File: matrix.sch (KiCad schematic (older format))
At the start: 126 parts

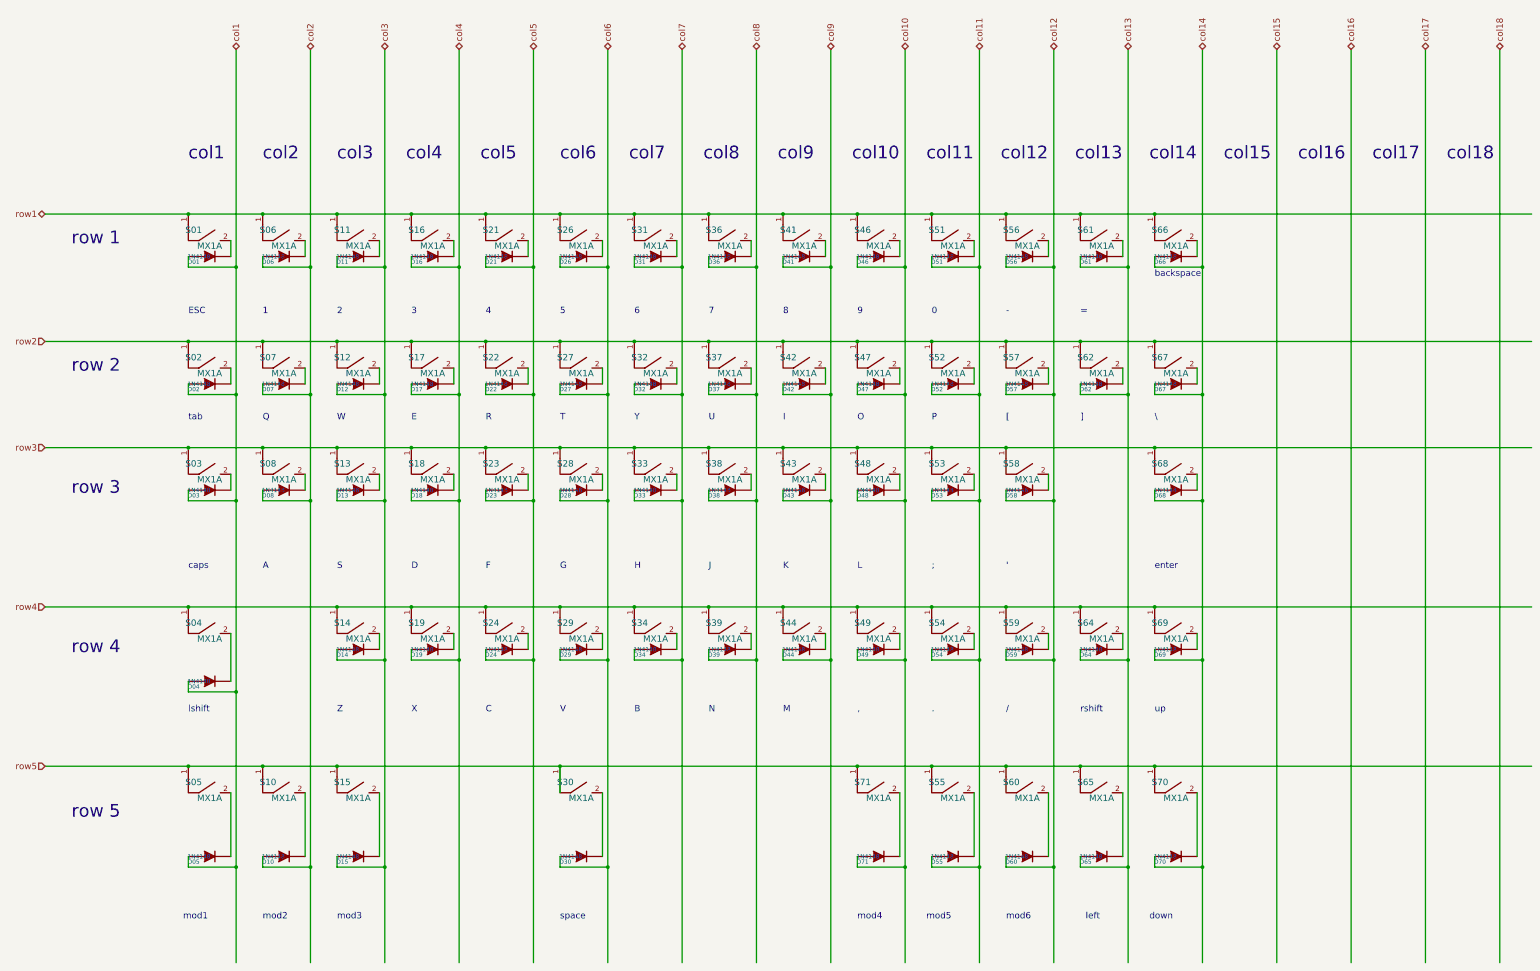
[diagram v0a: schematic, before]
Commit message: Optimise matrix to save an additional pin on the MCU
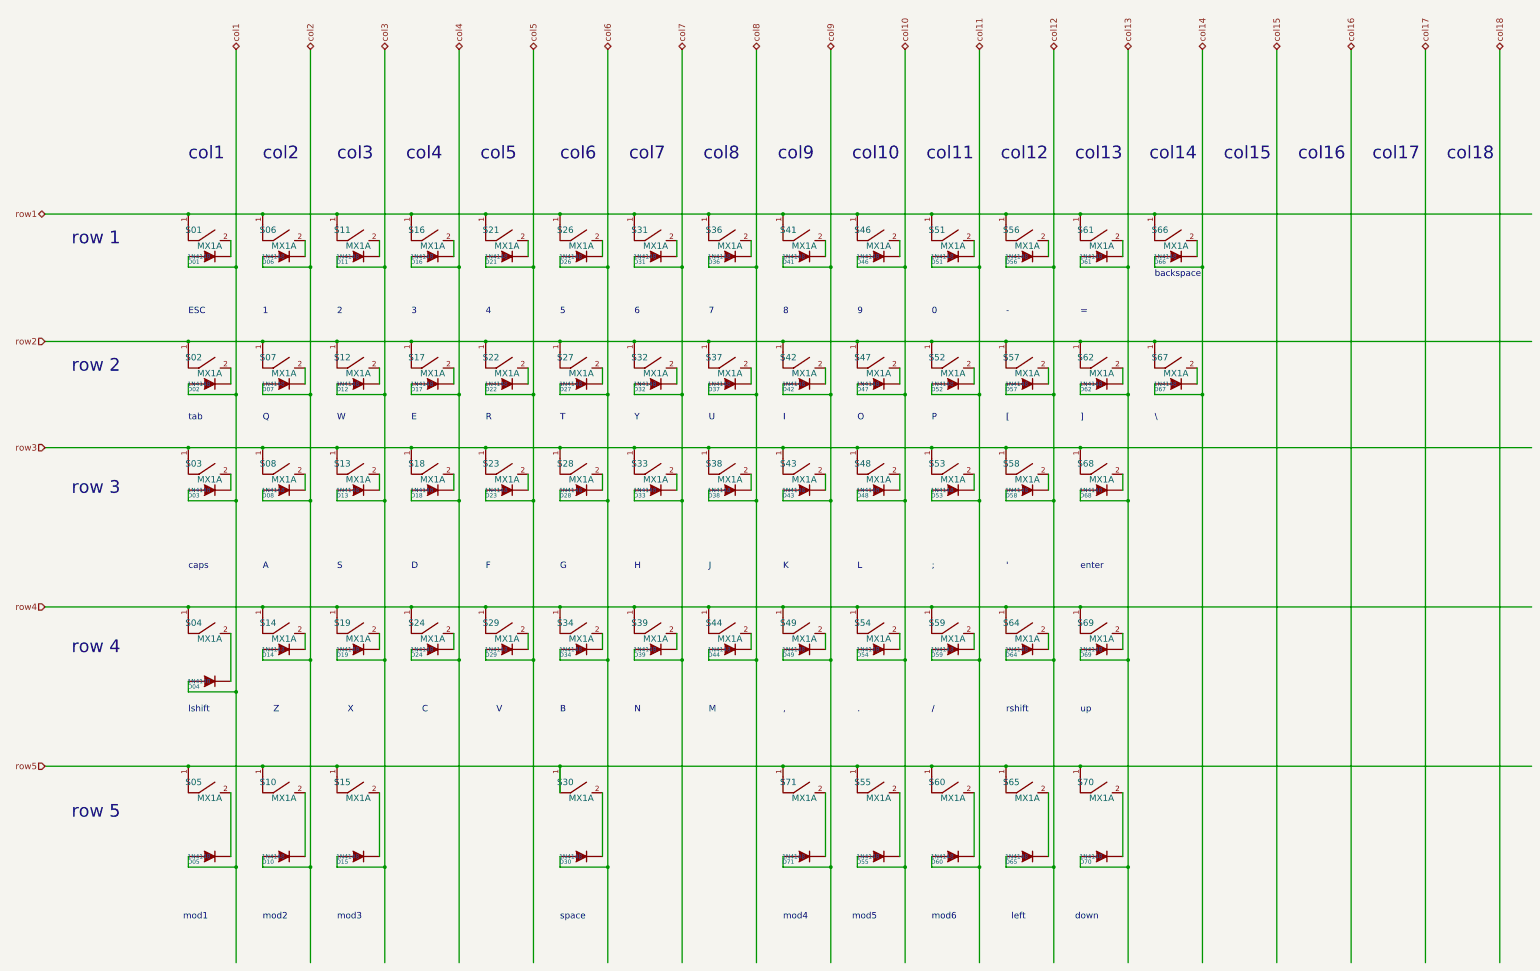
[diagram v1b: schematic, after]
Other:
- moved on the sheet: D14, D19, D24, D29, D34, D39, D44, D49, D54, D55, D59, D60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

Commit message: PCB with 3 pins ready for backlight
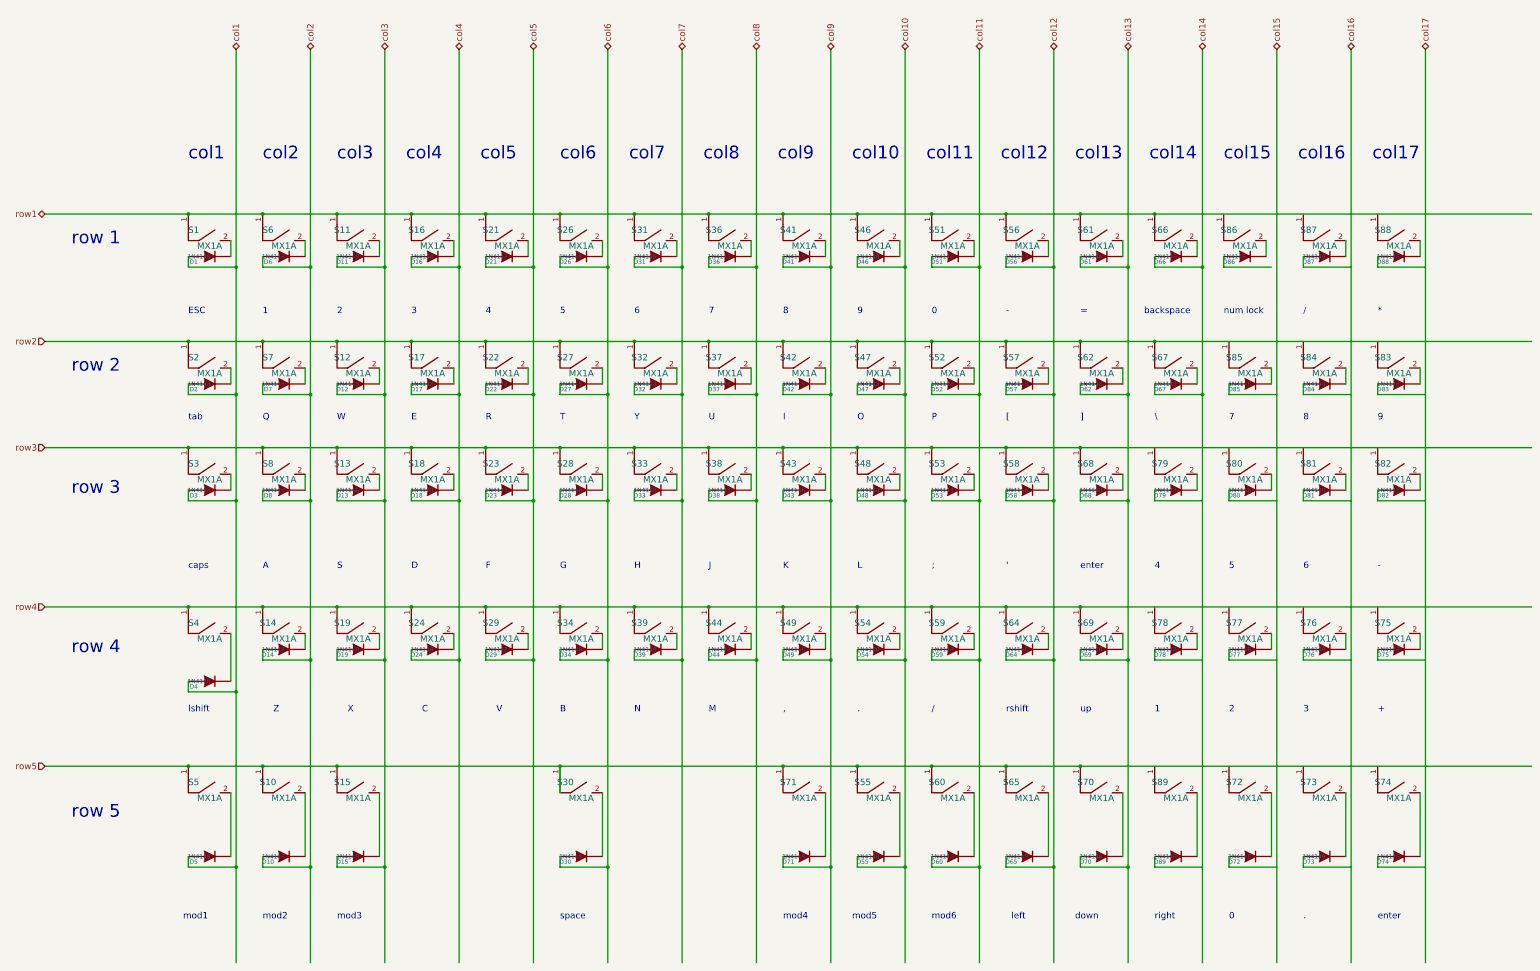
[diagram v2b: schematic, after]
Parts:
- added D72, D73, D74, D75, D76, D77, D78, D79, D80, D81, D82, D83, D84, D85, D86, D87, D88, D89: 1N4148, 0805:0805D, symbol device:DIODE
- added S72, S73, S74, S75, S76, S77, S78, S79, S80, S81, S82, S83, S84, S85, S86, S87, S88, S89: MX1A, mx1a:MX1A, symbol mx1a-simple:MX1A
- renumbered D01 to D1, D02 to D2, D03 to D3, D04 to D4, D05 to D5, D06 to D6, D07 to D7, D08 to D8, S01 to S1, S02 to S2, S03 to S3, S04 to S4, S05 to S5, S06 to S6, S07 to S7, S08 to S8
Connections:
- net labels removed: col18
- wire segments 339 -> 392
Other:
- note added: "*"
- note added: "+"
- note added: "num lock"
- note added: "right"
- note removed: "col18"

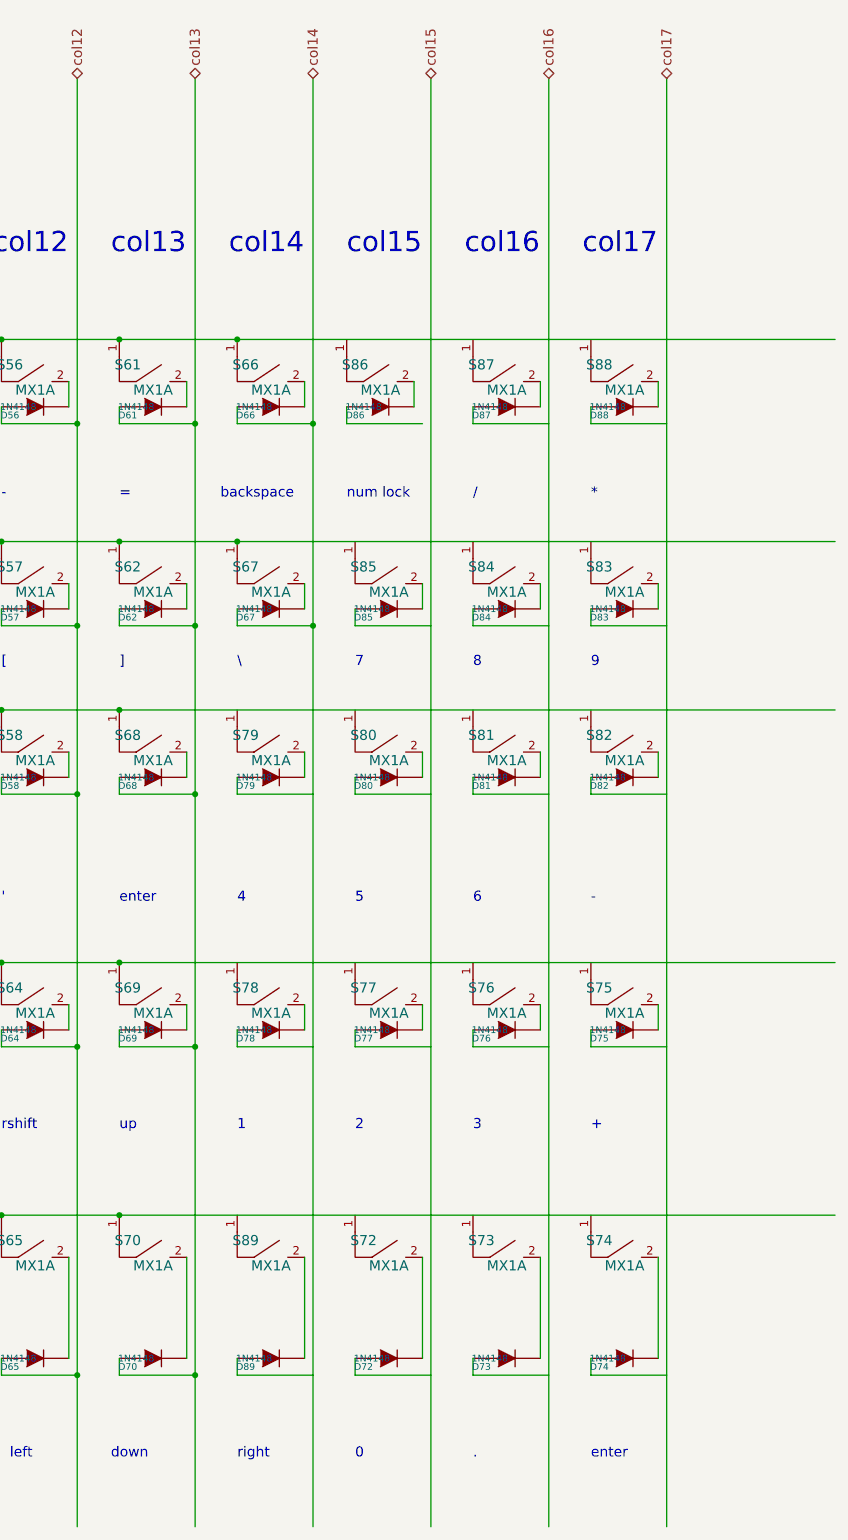
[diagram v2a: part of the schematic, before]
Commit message: Add all keys in PCB for numpad
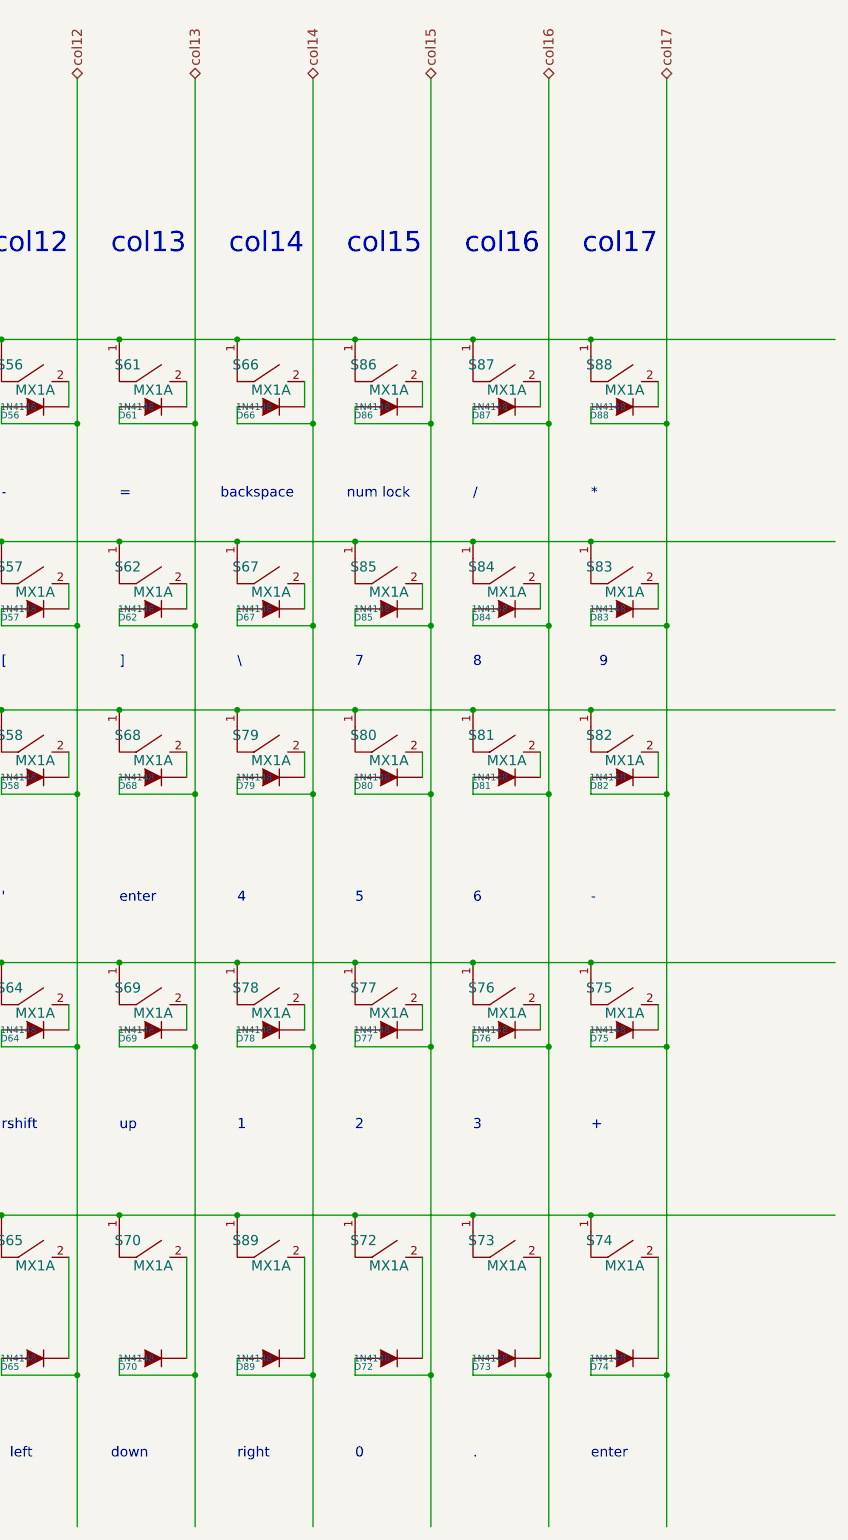
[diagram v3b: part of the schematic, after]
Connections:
- wire segments 392 -> 428
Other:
- moved on the sheet: D86, S86
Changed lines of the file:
@@
 col17
 Wire Wire Line
-	11500 2800 15050 2800
-Wire Wire Line
-	11500 4000 15050 4000
-Wire Wire Line
-	12650 1250 12650 9850
-Wire Wire Line
-	13350 1250 13350 9850
-Wire Wire Line
-	14050 1250 14050 9850
+	11500 2800 12200 2800
+Wire Wire Line
+	12650 1250 12650 3300
+Wire Wire Line
+	13350 1250 13350 3300
+Wire Wire Line
+	14050 1250 14050 3300
 Connection ~ 3100 6500
 Connection ~ 3550 7000
@@
 Connection ~ 11250 7000
 Wire Wire Line
-	10800 6500 15050 6500
+	10800 6500 11500 6500
 Connection ~ 8000 8000
 Connection ~ 8450 8950
@@
 	11250 8950 11250 9850
 Wire Wire Line
-	11950 4500 11950 9850
-Wire Wire Line
-	10800 8000 15050 8000
+	11950 4500 11950 5500
+Wire Wire Line
+	10800 8000 11500 8000
 $Comp
 L mx1a-simple:MX1A S89
@@
 $EndComp
 Wire Wire Line
-	10800 5000 15050 5000
-Wire Wire Line
 	10100 5000 10800 5000
 Connection ~ 10800 5000
@@
 L mx1a-simple:MX1A S86
 U 1 1 6240C9C2
-P 12350 3200
-F 0 "S86" H 12200 3450 60  0000 C CNN
-F 1 "MX1A" H 12350 3300 60  0000 C CNN
-F 2 "mx1a:MX1A" H 12350 3200 60  0001 C CNN
-F 3 "" H 12350 3200 60  0001 C CNN
-	1    12350 3200
+P 12400 3200
+F 0 "S86" H 12250 3450 60  0000 C CNN
+F 1 "MX1A" H 12400 3300 60  0000 C CNN
+F 2 "mx1a:MX1A" H 12400 3200 60  0001 C CNN
+F 3 "" H 12400 3200 60  0001 C CNN
+	1    12400 3200
 	1    0    0    -1
 $EndComp
@@
 L device:DIODE D86
 U 1 1 6240C9CC
-P 12350 3200
-F 0 "D86" H 12200 3150 40  0000 C CNN
-F 1 "1N4148" H 12250 3200 40  0000 C CNN
-F 2 "0805:0805D" H 12350 3200 60  0001 C CNN
-F 3 "" H 12350 3200 60  0001 C CNN
-F 4 "DC Components" H 5200 2600 60  0001 C CNN "Vendor"
-F 5 "CD4148WS(0805C)" H 5200 2600 60  0001 C CNN "Product"
-F 6 "TME" H 5200 2600 60  0001 C CNN "Supplier"
-F 7 "1N4148-0805" H 5200 2600 60  0001 C CNN "Supplier Symbol"
-	1    12350 3200
-	1    0    0    -1
-$EndComp
-Wire Wire Line
-	12150 3200 12150 3300
-Wire Wire Line
-	12150 3300 12600 3300
-Wire Wire Line
-	12550 3200 12550 3050
+P 12400 3200
+F 0 "D86" H 12250 3150 40  0000 C CNN
+F 1 "1N4148" H 12300 3200 40  0000 C CNN
+F 2 "0805:0805D" H 12400 3200 60  0001 C CNN
+F 3 "" H 12400 3200 60  0001 C CNN
+F 4 "DC Components" H 5250 2600 60  0001 C CNN "Vendor"
+F 5 "CD4148WS(0805C)" H 5250 2600 60  0001 C CNN "Product"
+F 6 "TME" H 5250 2600 60  0001 C CNN "Supplier"
+F 7 "1N4148-0805" H 5250 2600 60  0001 C CNN "Supplier Symbol"
+	1    12400 3200
+	1    0    0    -1
+$EndComp
+Wire Wire Line
+	12200 3200 12200 3300
+Wire Wire Line
+	12200 3300 12650 3300
+Wire Wire Line
+	12600 3200 12600 3050
 $Comp
 L mx1a-simple:MX1A S87
@@
 Text Notes 12900 4750 0    60   ~ 0
 8
-Text Notes 13600 4750 0    60   ~ 0
+Text Notes 13650 4750 0    60   ~ 0
 9
 Text Notes 12150 3750 0    60   ~ 0
@@
 Text Notes 13600 3750 0    60   ~ 0
 *
+Connection ~ 12200 2800
+Connection ~ 12650 3300
+Wire Wire Line
+	12650 3300 12650 4500
+Connection ~ 12900 2800
+Connection ~ 13350 3300
+Wire Wire Line
+	13350 3300 13350 4500
+Wire Wire Line
+	12200 2800 12900 2800
+Connection ~ 13600 2800
+Wire Wire Line
+	13600 2800 15050 2800
+Connection ~ 14050 3300
+Wire Wire Line
+	14050 3300 14050 4500
+Wire Wire Line
+	12900 2800 13600 2800
+Connection ~ 13600 4000
+Wire Wire Line
+	13600 4000 15050 4000
+Connection ~ 14050 4500
+Wire Wire Line
+	14050 4500 14050 5500
+Connection ~ 12900 4000
+Wire Wire Line
+	12900 4000 13600 4000
+Connection ~ 13350 4500
+Wire Wire Line
+	13350 4500 13350 5500
+Wire Wire Line
+	11500 4000 12200 4000
+Connection ~ 12200 4000
+Wire Wire Line
+	12200 4000 12900 4000
+Connection ~ 12650 4500
+Wire Wire Line
+	12650 4500 12650 5500
+Connection ~ 13600 5000
+Wire Wire Line
+	13600 5000 15050 5000
+Connection ~ 14050 5500
+Wire Wire Line
+	14050 5500 14050 7000
+Connection ~ 12900 5000
+Wire Wire Line
+	12900 5000 13600 5000
+Connection ~ 13350 5500
+Wire Wire Line
+	13350 5500 13350 7000
+Connection ~ 12200 5000
+Wire Wire Line
+	12200 5000 12900 5000
+Connection ~ 12650 5500
+Wire Wire Line
+	12650 5500 12650 7000
+Connection ~ 11500 5000
+Wire Wire Line
+	11500 5000 12200 5000
+Connection ~ 11950 5500
+Wire Wire Line
+	11950 5500 11950 7000
+Wire Wire Line
+	10800 5000 11500 5000
+Connection ~ 11500 6500
+Wire Wire Line
+	11500 6500 12200 6500
+Connection ~ 11950 7000
+Wire Wire Line
+	11950 7000 11950 8950
+Connection ~ 12200 6500
+Wire Wire Line
+	12200 6500 12900 6500
+Connection ~ 12650 7000
+Wire Wire Line
+	12650 7000 12650 8950
+Connection ~ 12900 6500
+Wire Wire Line
+	12900 6500 13600 6500
+Connection ~ 13350 7000
+Wire Wire Line
+	13350 7000 13350 8950
+Connection ~ 13600 6500
+Wire Wire Line
+	13600 6500 15050 6500
+Connection ~ 14050 7000
+Wire Wire Line
+	14050 7000 14050 8950
+Connection ~ 11500 8000
+Wire Wire Line
+	11500 8000 12200 8000
+Connection ~ 12200 8000
+Wire Wire Line
+	12200 8000 12900 8000
+Connection ~ 12900 8000
+Wire Wire Line
+	12900 8000 13600 8000
+Connection ~ 13600 8000
+Wire Wire Line
+	13600 8000 15050 8000
+Connection ~ 14050 8950
+Wire Wire Line
+	14050 8950 14050 9850
+Connection ~ 13350 8950
+Wire Wire Line
+	13350 8950 13350 9850
+Connection ~ 12650 8950
+Wire Wire Line
+	12650 8950 12650 9850
+Connection ~ 11950 8950
+Wire Wire Line
+	11950 8950 11950 9850
 $EndSCHEMATC

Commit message: Update footprint in matrix
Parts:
- S64: footprint mx1a:MX1A_no3d -> mx1a:MX1A
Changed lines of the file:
@@
 F 0 "S64" H 10150 7150 60  0000 C CNN
 F 1 "MX1A" H 10300 7000 60  0000 C CNN
-F 2 "mx1a:MX1A_no3d" H 10300 6900 60  0001 C CNN
+F 2 "mx1a:MX1A" H 10300 6900 60  0001 C CNN
 F 3 "" H 10300 6900 60  0001 C CNN
 	1    10300 6900

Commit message: Update BOM in schematic and matrix
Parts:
- D1, D10, D11, D12, D13, D14, D15, D16, D17, D18, D19, D2, D21, D22, D23, D24, D26, D27, D28, D29, D3, D30, D31, D32, D33, D34, D36, D37, D38, D39, D4, D41, D42, D43, D44, D46, D47, D48, D49, D5, D51, D52, D53, D54, D55, D56, D57, D58, D59, D6, D60, D61, D62, D64, D65, D66, D67, D68, D69, D7, D70, D71, D72, D73, D74, D75, D76, D77, D78, D79, D8, D80, D81, D82, D83, D84, D85, D86, D87, D88, D89: LCSC (none) -> C109001

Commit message: Change diode footprint
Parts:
- D1, D10, D11, D12, D13, D14, D15, D16, D17, D18, D19, D2, D21, D22, D23, D24, D26, D27, D28, D29, D3, D30, D31, D32, D33, D34, D36, D37, D38, D39, D4, D41, D42, D43, D44, D46, D47, D48, D49, D5, D51, D52, D53, D54, D55, D56, D57, D58, D59, D6, D60, D61, D62, D64, D65, D66, D67, D68, D69, D7, D70, D71, D72, D73, D74, D75, D76, D77, D78, D79, D8, D80, D81, D82, D83, D84, D85, D86, D87, D88, D89: footprint 0805:0805D -> Diode_SMD:D_SOD-323F; LCSC C109001 -> C2128
